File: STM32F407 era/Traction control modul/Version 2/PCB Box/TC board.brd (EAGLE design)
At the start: 127 x 165.1 mm, 161 parts, among them IC2 lm2575, IC5 REG1117, J1 CON1, J2 CON1, U1 MAX13052ESA+, U2 MAX232AEWE+, U3 MAX531AESD+, U5 MAX9926, U6 MAX9926, U7 HEF4049BT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

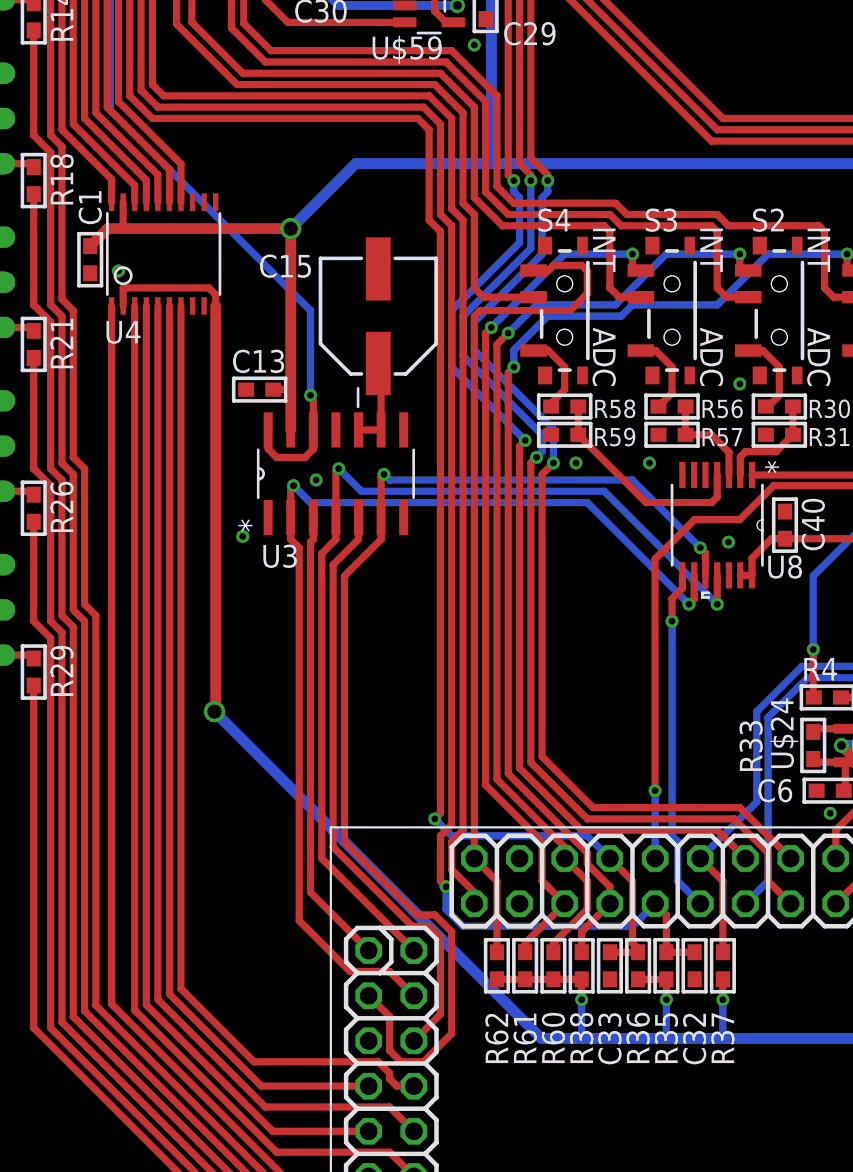
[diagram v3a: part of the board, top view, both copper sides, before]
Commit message: replaced DAC for better
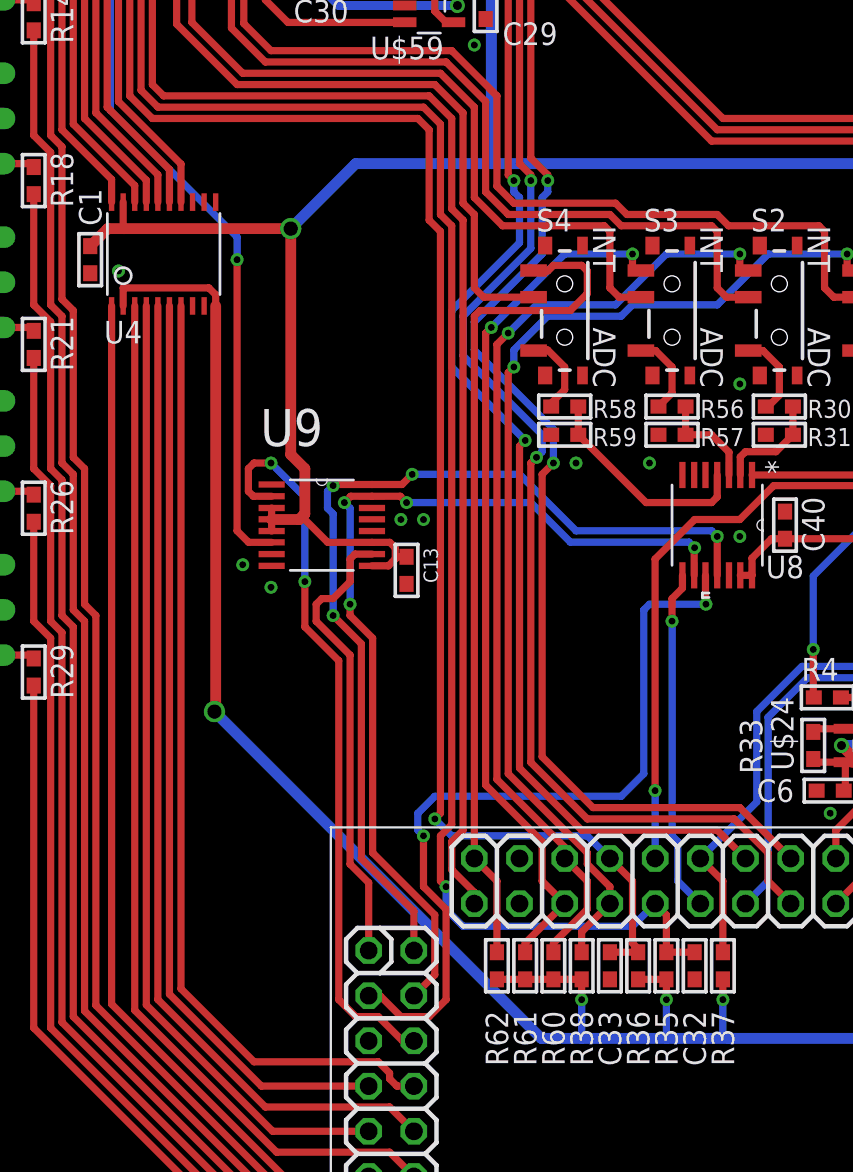
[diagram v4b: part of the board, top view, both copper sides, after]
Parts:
- removed C15: 33uf pan FC, microbuilder:PANASONIC_D
- removed U3: MAX531AESD+, Maxim_By_element14_Batch_1:SOIC127P600X175-14N
- added U9: AD5024BRUZ, AAU-Racing:SOP65P640X120-16N
- moved C13 13.1 mm to (49.2, 81.3), turned to 270 degrees
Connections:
- removed net REF: C15.+, U3.10, U3.9
- new net LDAC: U9.1
- net 5.0V: now also U9.11, U9.3, U9.4, U9.5, U9.9; no longer U3.13
- net DACCLR: now also U9.10; no longer U3.3
- net DACCS: now also U9.2; no longer U3.5
- net GND: now also U9.14, U9.8; no longer C15.-, U3.1, U3.11, U3.7, U3.8
- net MISO: no longer U3.6
- net MOSI: now also U9.15; no longer U3.2
- net SCK: now also U9.16; no longer U3.4
- net VOUT: now also U9.6; no longer U3.12, U3.14
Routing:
- net MISO: track 64.5 -> 44.5 mm
- net 5.0V: track 260.3 -> 276.4 mm
- net DACCS: track 33.7 -> 41.0 mm, vias 0 -> 2
- net REF: track 7.24 -> 0.00 mm
- net MOSI: track 59.6 -> 52.9 mm, vias 2 -> 4
- net SCK: track 55.7 -> 53.8 mm, vias 2 -> 4
- net VOUT: track 63.8 -> 64.8 mm
- net GND: vias 25 -> 27

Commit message: I dont remember
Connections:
- net RPM4: now also U$1.P$53; no longer U$1.P$47
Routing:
- net RPM4: track 85.1 -> 100.8 mm
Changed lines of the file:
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@@
 </signal>
 <signal name="RPM4">
-<contactref element="U$1" pad="P$47"/>
 <contactref element="U7" pad="2"/>
 <wire x1="117.1575" y1="80.0608" x2="117.1575" y2="79.0575" width="0.4064" layer="1"/>
@@
 <wire x1="115.8875" y1="33.3375" x2="111.76" y2="29.21" width="0.4064" layer="1"/>
 <wire x1="111.76" y1="29.21" x2="103.505" y2="29.21" width="0.4064" layer="1"/>
-<wire x1="86.741" y1="18.7325" x2="93.0275" y2="18.7325" width="0.4064" layer="1"/>
 <wire x1="93.0275" y1="18.7325" x2="103.505" y2="29.21" width="0.4064" layer="1"/>
+<contactref element="U$1" pad="P$53"/>
+<wire x1="93.0275" y1="18.7325" x2="88.5825" y2="18.7325" width="0.4064" layer="1"/>
+<wire x1="88.5825" y1="18.7325" x2="87.3125" y2="17.4625" width="0.4064" layer="1"/>
+<wire x1="87.3125" y1="17.4625" x2="83.5025" y2="17.4625" width="0.4064" layer="1"/>
+<wire x1="83.5025" y1="17.4625" x2="82.8675" y2="18.0975" width="0.4064" layer="1"/>
+<wire x1="82.8675" y1="18.0975" x2="82.8675" y2="24.4475" width="0.4064" layer="1"/>
+<wire x1="82.8675" y1="24.4475" x2="83.5025" y2="25.0825" width="0.4064" layer="1"/>
+<wire x1="83.5025" y1="25.0825" x2="85.09" y2="25.0825" width="0.4064" layer="1"/>
+<wire x1="85.09" y1="25.0825" x2="85.725" y2="25.7175" width="0.4064" layer="1"/>
+<wire x1="85.725" y1="25.7175" x2="86.106" y2="25.7175" width="0.4064" layer="1"/>
+<wire x1="86.106" y1="25.7175" x2="86.741" y2="26.3525" width="0.4064" layer="1"/>
 </signal>
 <signal name="CAN_RX">
@@
 <contactref element="U2" pad="9"/>
 <contactref element="U$1" pad="P$52"/>
-<wire x1="84.201" y1="23.8125" x2="85.471" y2="25.0825" width="0.4064" layer="1"/>
-<wire x1="85.471" y1="25.0825" x2="92.3925" y2="25.0825" width="0.4064" layer="1"/>
 <wire x1="101.12375" y1="33.81375" x2="101.12375" y2="35.14725" width="0.4064" layer="1"/>
 <wire x1="92.3925" y1="25.0825" x2="101.12375" y2="33.81375" width="0.4064" layer="1"/>
+<wire x1="84.201" y1="23.8125" x2="84.7725" y2="23.8125" width="0.4064" layer="1"/>
+<wire x1="84.7725" y1="23.8125" x2="86.0425" y2="25.0825" width="0.4064" layer="1"/>
+<wire x1="86.0425" y1="25.0825" x2="92.3925" y2="25.0825" width="0.4064" layer="1"/>
 </signal>
 <signal name="COMTX">

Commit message: minor updates to power circuitry
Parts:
- removed D2: 1n5824, diode:DO201-15
- added D8: (no value), diode:SMC
- added TP1, TP2, TP3: (no value), microbuilder:TESTPOINT_ROUND_2MM
- added TP4: (no value), microbuilder:TESTPOINT_SMT
- added X1: (no value), con-molex:22-23-2021
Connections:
- removed net LDAC: U9.1
- net 12V: now also TP1.P$1, X1.1
- net 3.3V: now also TP3.P$1
- net 5.0V: now also TP2.P$1
- net GND: now also D8.A, TP4.P$1, U9.1, X1.2; no longer D2.A
- net N$2: now also D8.C; no longer D2.C
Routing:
- net 12V: track 81.3 -> 100.7 mm
- net N$2: track 28.7 -> 21.3 mm
- net 5.0V: track 276.4 -> 282.6 mm
- net 3.3V: track 716.6 -> 719.1 mm, vias 33 -> 32
- net BRAKE-POTB: track 82.8 -> 82.2 mm
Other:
- board text added: "+"
- board text added: "12V"
- board text added: "3,3V"
- board text added: "5V"
- board text added: "AUX POWER"
- board text added: "GND"

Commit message: added testpoints to power rails and coms, and created new Gerbers for PCB order
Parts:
- added JP1: SPI, pinhead:1X03
- TP1, TP2, TP3: device microbuilder:TESTPOINT_ROUND_2MM -> microbuilder:TESTPOINT_SMT
- moved TP3 0.32 mm to (76.8, 119.1)
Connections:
- removed net AUX1: J1.D1
- removed net SCL: U$1.P$58
- removed net SDA: U$1.P$57
- net MISO: now also JP1.1
- net MOSI: now also JP1.2
- net SCK: now also JP1.3
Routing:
- net SCK: track 53.8 -> 62.7 mm
- net MOSI: track 52.9 -> 61.8 mm
- net MISO: track 44.5 -> 50.8 mm
- net 12V: track 100.7 -> 101.2 mm
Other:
- board text added: "MISO"
- board text added: "MOSI"
- board text added: "SCK"
- board text added: "SPI"
